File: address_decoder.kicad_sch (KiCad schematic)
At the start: 9 parts, among them J1 Conn_02x04_Counter_Clockwise, U2 74LS138, U3 74LS245, U4 74LS08, U5 74LS02, U6 74LS00, U7 PAL16L8, U8 74LS08

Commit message: Update circuit
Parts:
- added U10: 74LS244_Split, symbol 74xx:74LS244_Split
- added U9: 74LS125, symbol 74xx:74LS125
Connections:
- net at U8.4: now also U10.11, U10.14, U9.9
- net at U8.5: now also U10.12, U10.13, U9.5
- new net ~{DMAC_I/OR}: U10.6
- new net ~{DMAC_I/OW}: U10.8

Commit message: Add known pins
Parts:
- added R1: 10k, symbol Device:R
- J1: value Conn_02x04_Counter_Clockwise -> SW7; Location (none) -> 20C
- U10, U9: Location (none) -> 20F
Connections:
- net +5V: now also R1.1
- net SASI_CONFIG: now also R1.2
- net PL499_13: now reaches U5.3
- net PL501A_13: now reaches U4.2
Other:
- moved on the sheet: J1, U10A, U10B

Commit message: Add even more pins
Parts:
- added U1 (x9): 74F241_Split, symbol 74xx:74LS241_Split
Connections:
- net at U7.1 (I_{0}): now also U1.18
- net SASI_INTERFACE renamed L1_SASI_INTERFACE
- new net: U1.18, U1.2
- new net L1_UNKNOWN: U1.2

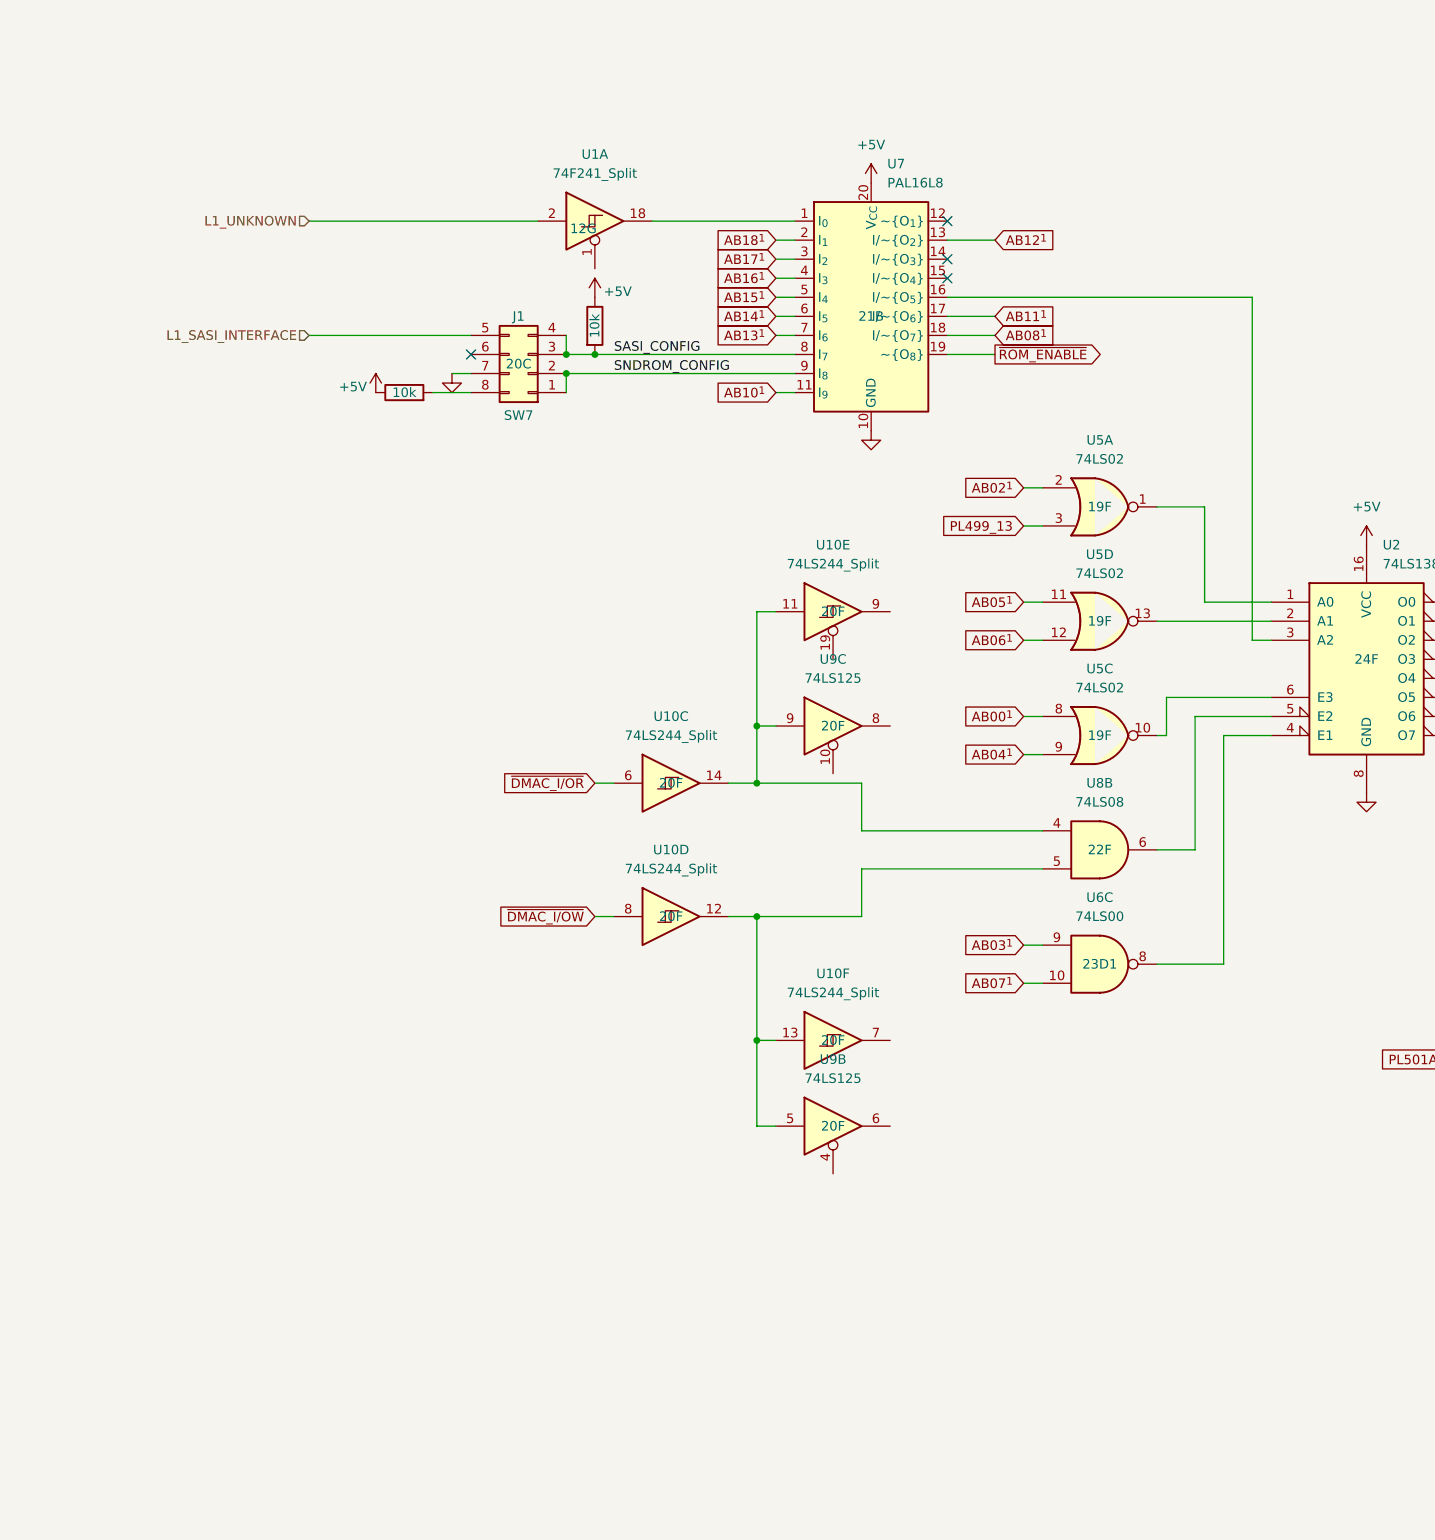
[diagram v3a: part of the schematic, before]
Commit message: Add address decoder description
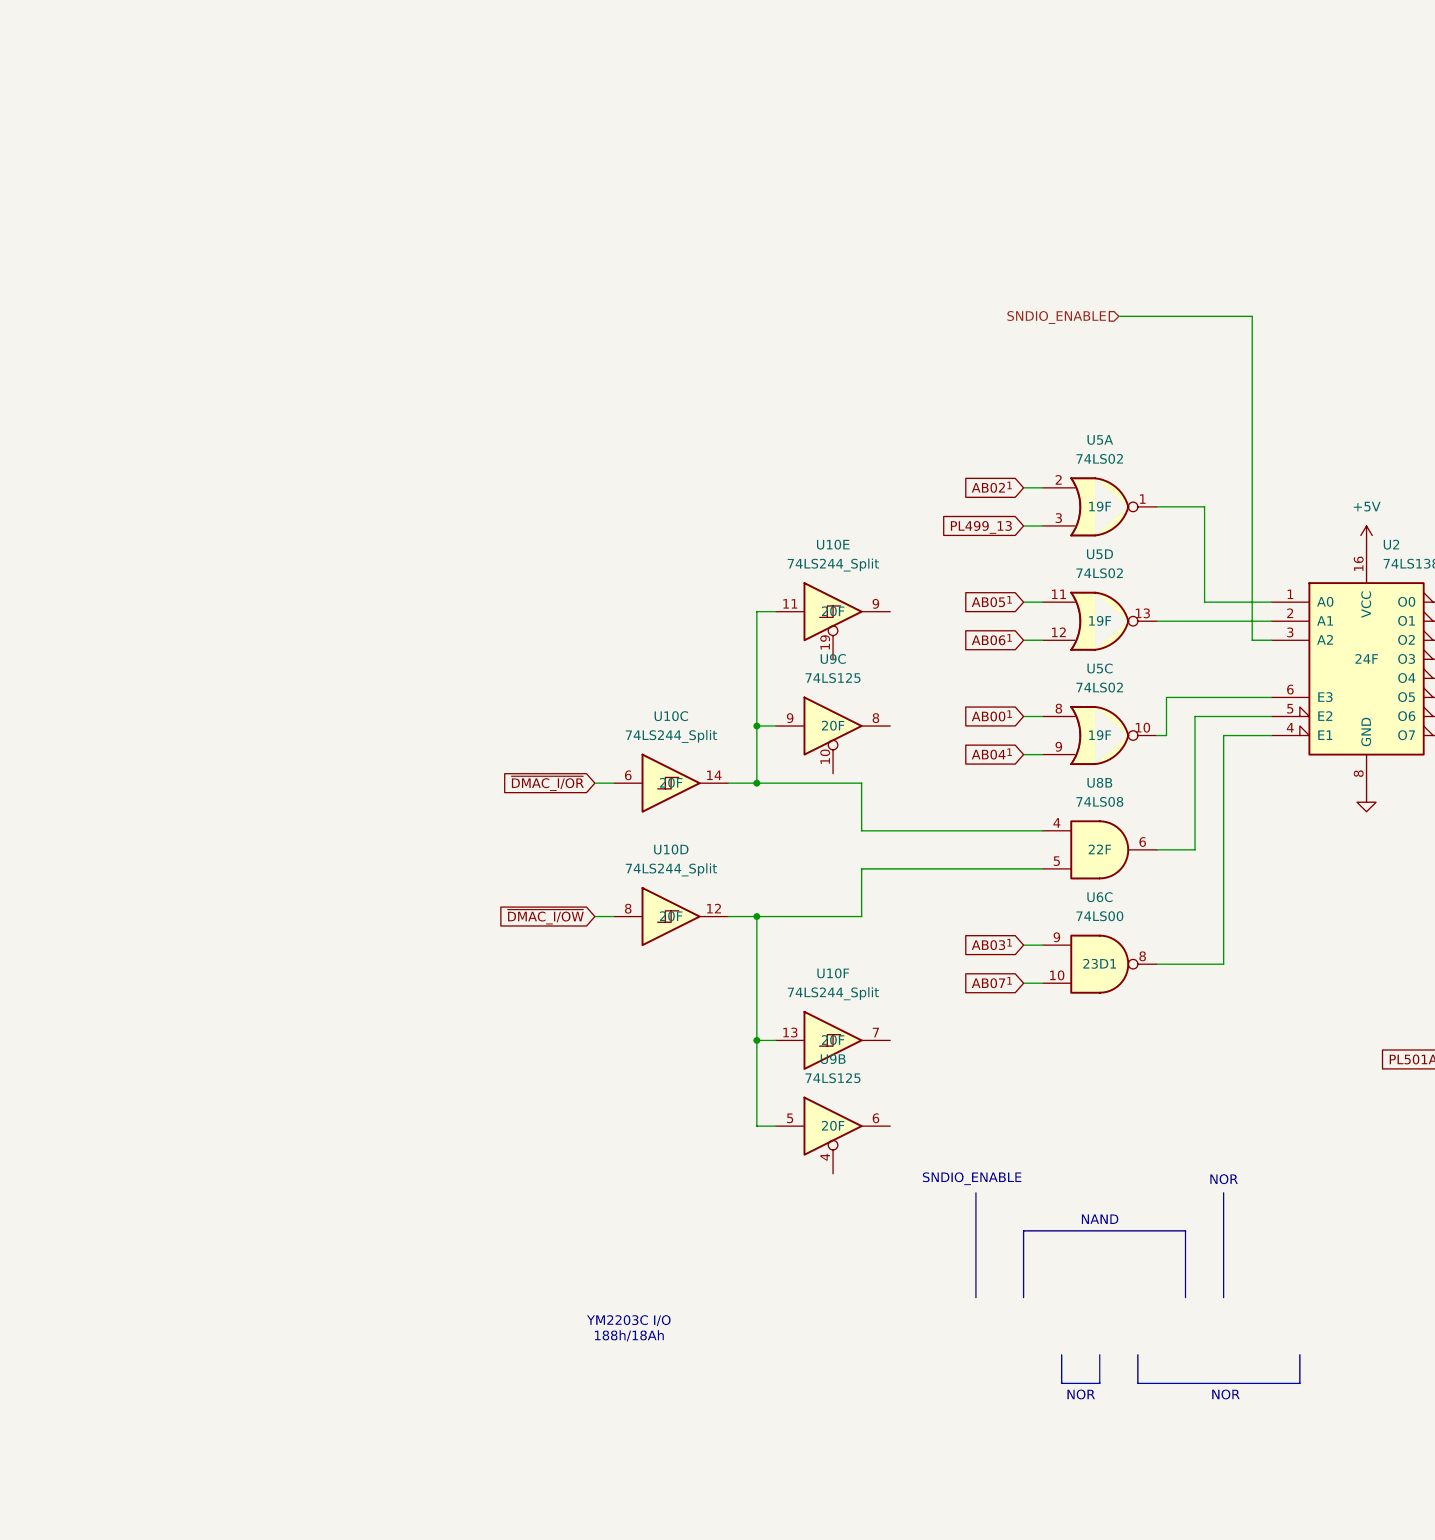
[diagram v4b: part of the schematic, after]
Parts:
- removed J1: SW7, symbol Connector_Generic:Conn_02x04_Counter_Clockwise
- removed R1 (x2): 10k, symbol Device:R
- removed U1: 74F241_Split, symbol 74xx:74LS241_Split
- removed U7: PAL16L8, symbol Logic_Programmable:PAL16L8
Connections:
- net SNDIO_ENABLE: now reaches U2.3 (A2)
- no-connect marks 11 -> 7
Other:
- note added: "NAND"
- note added: "NOR"
- note added: "SNDIO_ENABLE"
- note added: "YM2203C I/O 188h/18Ah"

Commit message: Add description
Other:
- note added: "NAND E_{1}"
- note added: "NOR A_{0}"
- note added: "NOR A_{1}"
- note added: "NOR E_{3}"
- note added: "SNDIO_ENABLE A_{2}"
- note removed: "NAND"
- note removed: "NOR"
- note removed: "SNDIO_ENABLE"
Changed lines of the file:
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@@
 	(generator_version "9.0")
 	(paper "A4")
-	(text "NAND"
+	(text "NAND E_{1}"
 		(exclude_from_sim no)
 		(at 143.51 167.64 0)
@@
 		)
 	)
-	(text "NOR"
+	(text "NOR A_{1}"
 		(exclude_from_sim no)
 		(at 140.97 191.008 0)
@@
 		)
 	)
-	(text "NOR"
+	(text "NOR A_{0}"
 		(exclude_from_sim no)
 		(at 160.02 162.306 0)
@@
 		)
 	)
-	(text "SNDIO_ENABLE"
+	(text "SNDIO_ENABLE A_{2}"
 		(exclude_from_sim no)
 		(at 126.492 162.052 0)
@@
 		)
 	)
-	(text "NOR"
+	(text "NOR E_{3}"
 		(exclude_from_sim no)
 		(at 160.274 191.008 0)
@@
 		)
 	)
+	(text_box "~{O7} = A0·A1·A2·E3·~{E2}·~{E1}"
+		(exclude_from_sim no)
+		(at 195.58 80.01 0)
+		(size 27.94 3.81)
+		(margins 0.9525 0.9525 0.9525 0.9525)
+		(stroke
+			(width 0)
+			(type solid)
+		)
+		(fill
+			(type none)
+		)
+		(effects
+			(font
+				(size 1.27 1.27)
+			)
+			(justify left top)
+		)
+	)
